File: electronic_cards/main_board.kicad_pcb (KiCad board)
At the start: 2 copper layers, 129 x 100 mm, 9 parts, among them J1 Input1, J2 Input2, J3 Esp8266, J4 Vin, J5 IN 5V, J6 Output1, J7 Output2

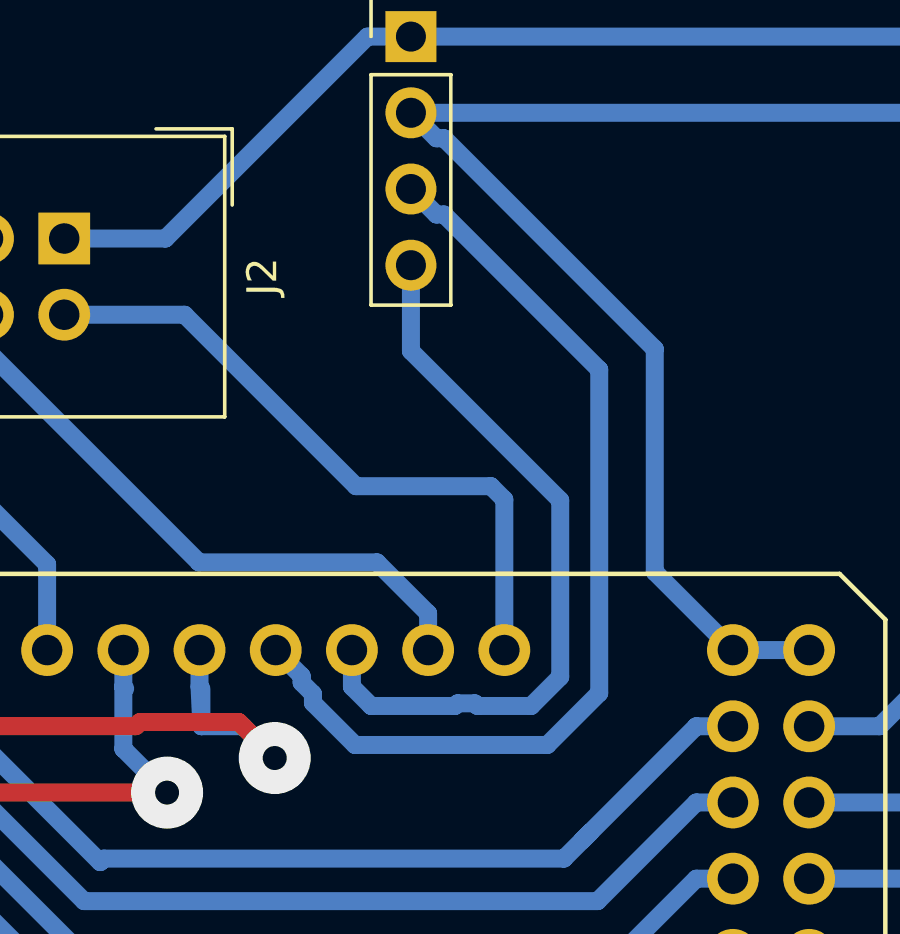
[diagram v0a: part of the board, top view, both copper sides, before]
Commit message: Correctrion of PCB, RX and TX of ESP were inverted
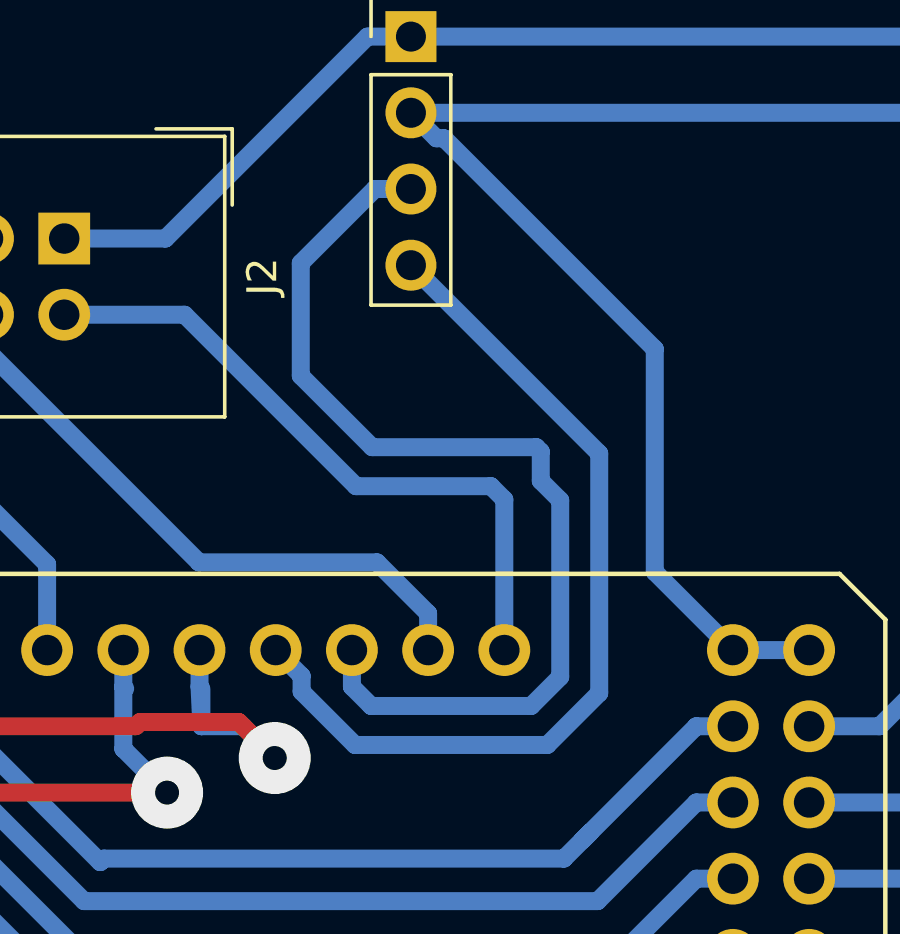
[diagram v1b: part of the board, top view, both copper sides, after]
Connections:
- XA1 pad D18: Net-(J3-Pad3) -> Net-(J3-Pad4)
- XA1 pad D19: Net-(J3-Pad4) -> Net-(J3-Pad3)
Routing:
- net Net-(J3-Pad4): track 24.7 -> 30.0 mm
- net Net-(J3-Pad3): track 32.7 -> 34.1 mm
